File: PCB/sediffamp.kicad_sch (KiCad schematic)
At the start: 19 parts, among them U4 OPA1622

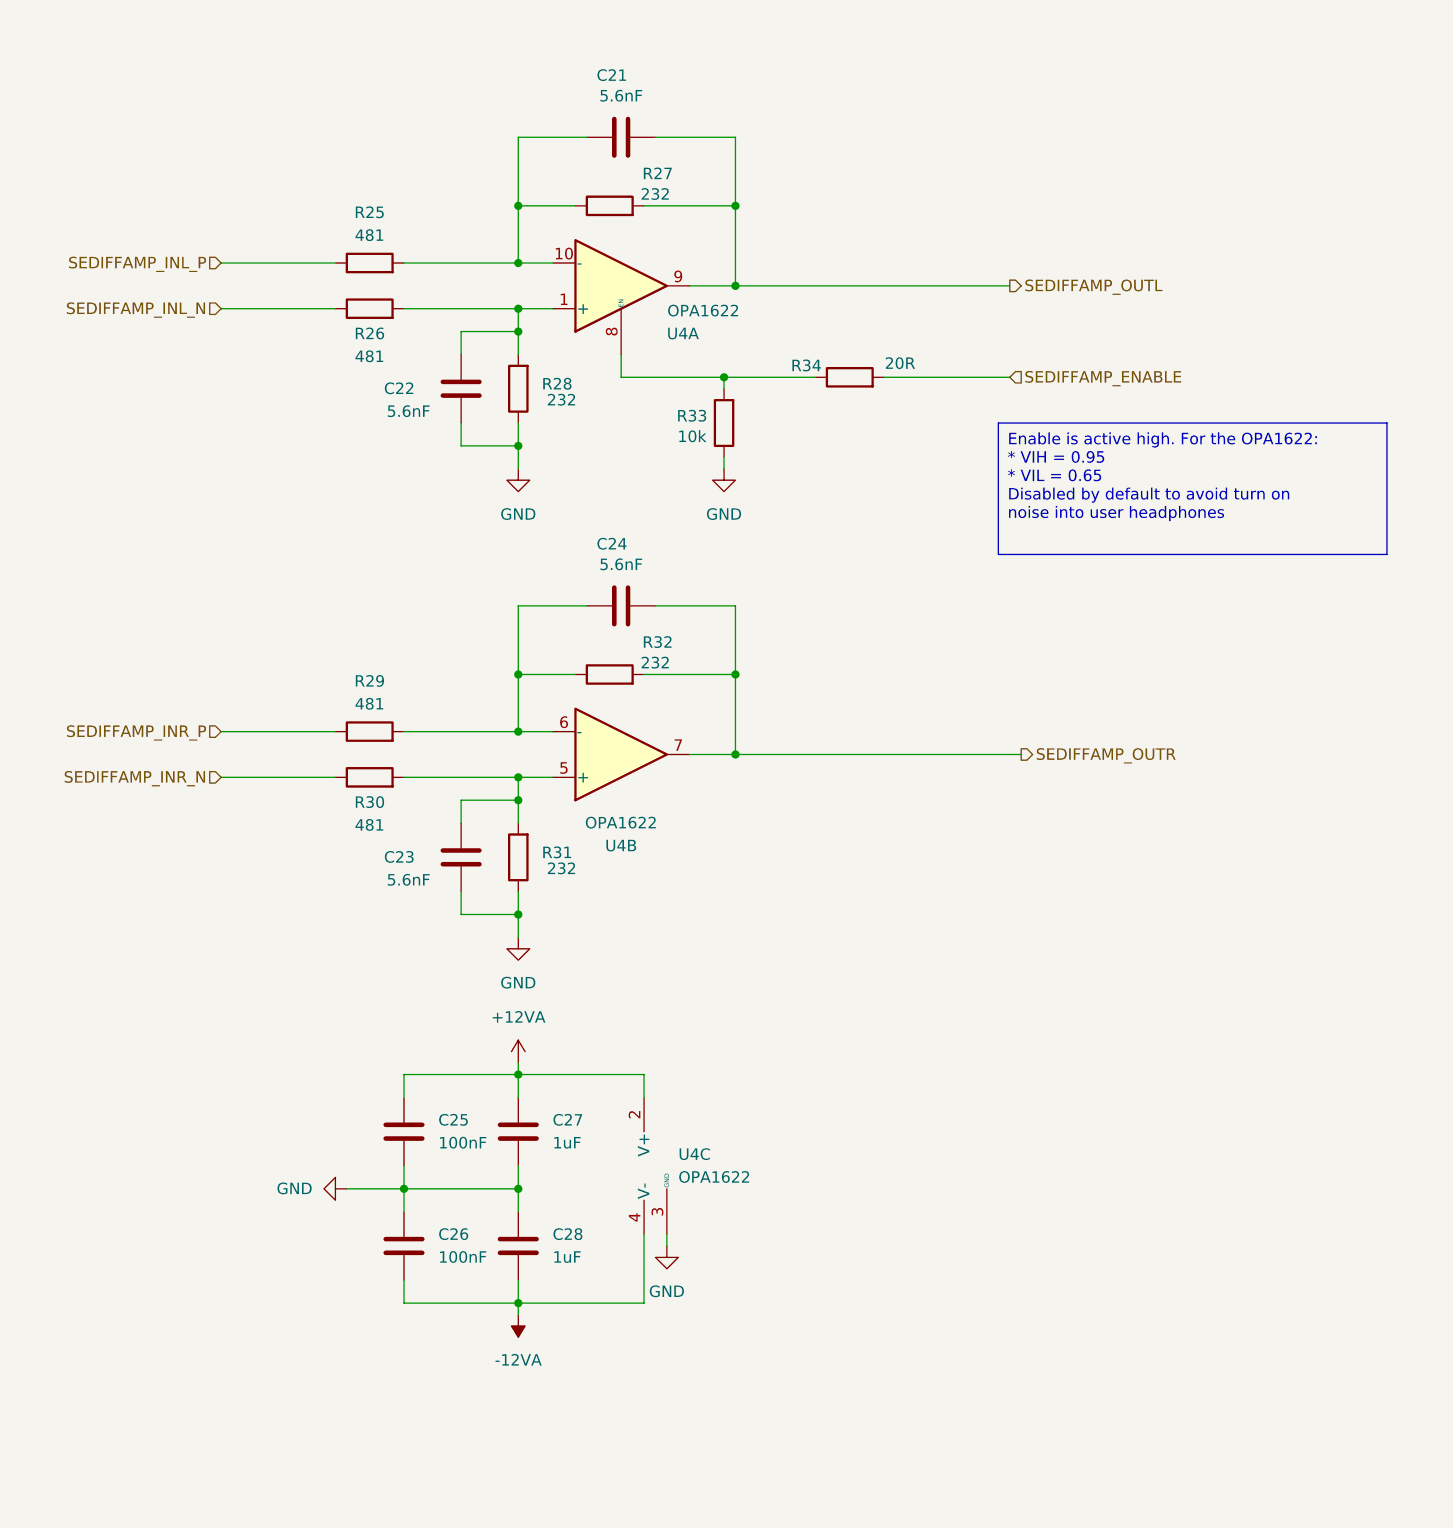
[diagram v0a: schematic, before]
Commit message: Added power supply and adjusted the AMP section to use only OPA1622 as output amp. In sync with Live 16
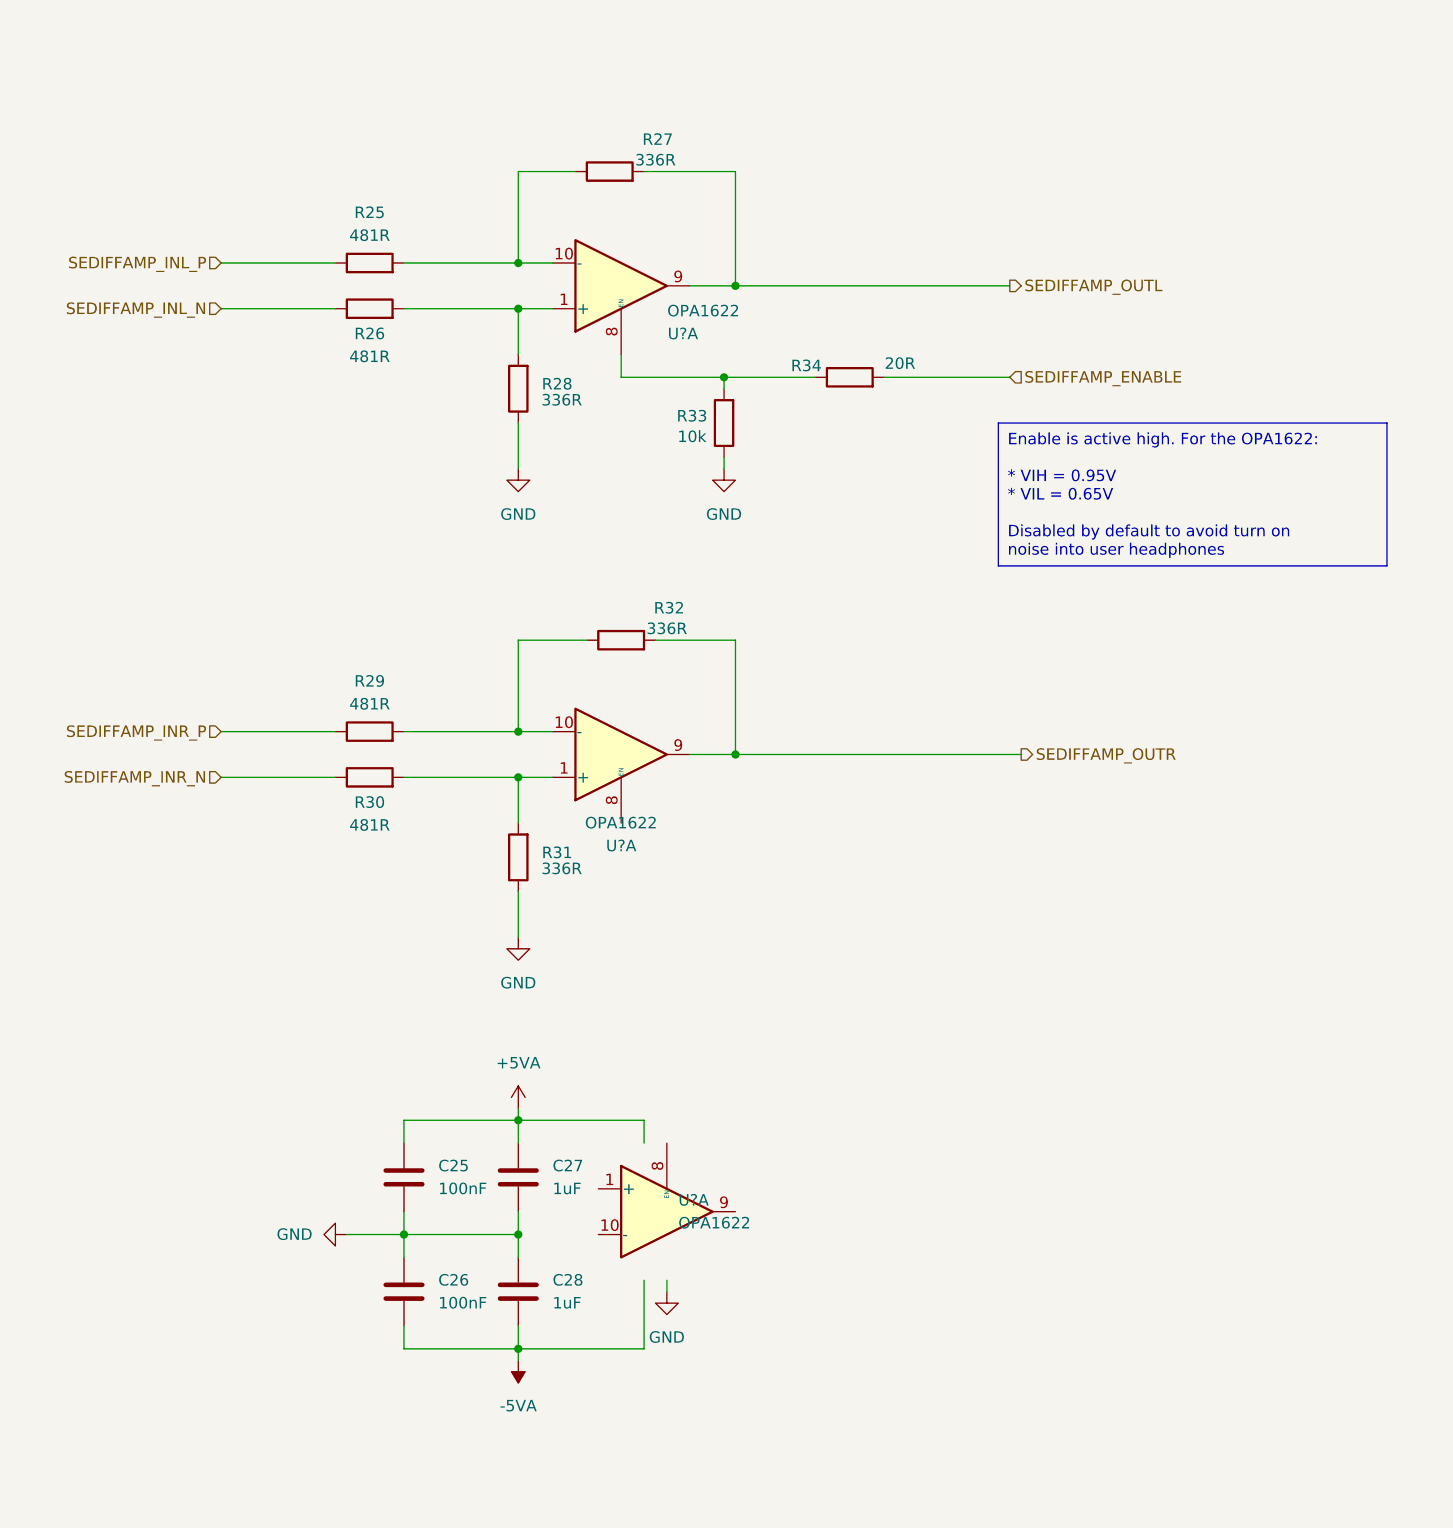
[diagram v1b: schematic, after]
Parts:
- removed C21, C22, C23, C24: 5.6nF, Capacitor_SMD:C_0402_1005Metric_Pad0.74x0.62mm_HandSolder, symbol Device:C
- C25, C26: Voltage 6.3V -> 25V
- R25, R26, R29, R30: value 481 -> 481R; Tolerance (none) -> 0.1%
- R27, R28, R31, R32: value 232 -> 336R; Tolerance (none) -> 0.1%
- renumbered U4 to U?
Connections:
- net GND: no longer U?.3 (GND)
- net SEDIFFAMP_OUTR: now also U?.9; no longer U?.7
- net at R30.2, R31.2: now also U?.1 (+); no longer U?.5 (+)
- net at R29.2, R32.1: now also U?.10 (-); no longer U?.6 (-)
- net +12VA renamed +5VA
- net +5VA: no longer U?.2 (V+)
- net -12VA renamed -5VA
- net -5VA: no longer U?.11 (V-), U?.4 (V-)
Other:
- moved on the sheet: C25, C26, C27, C28, R27, R32

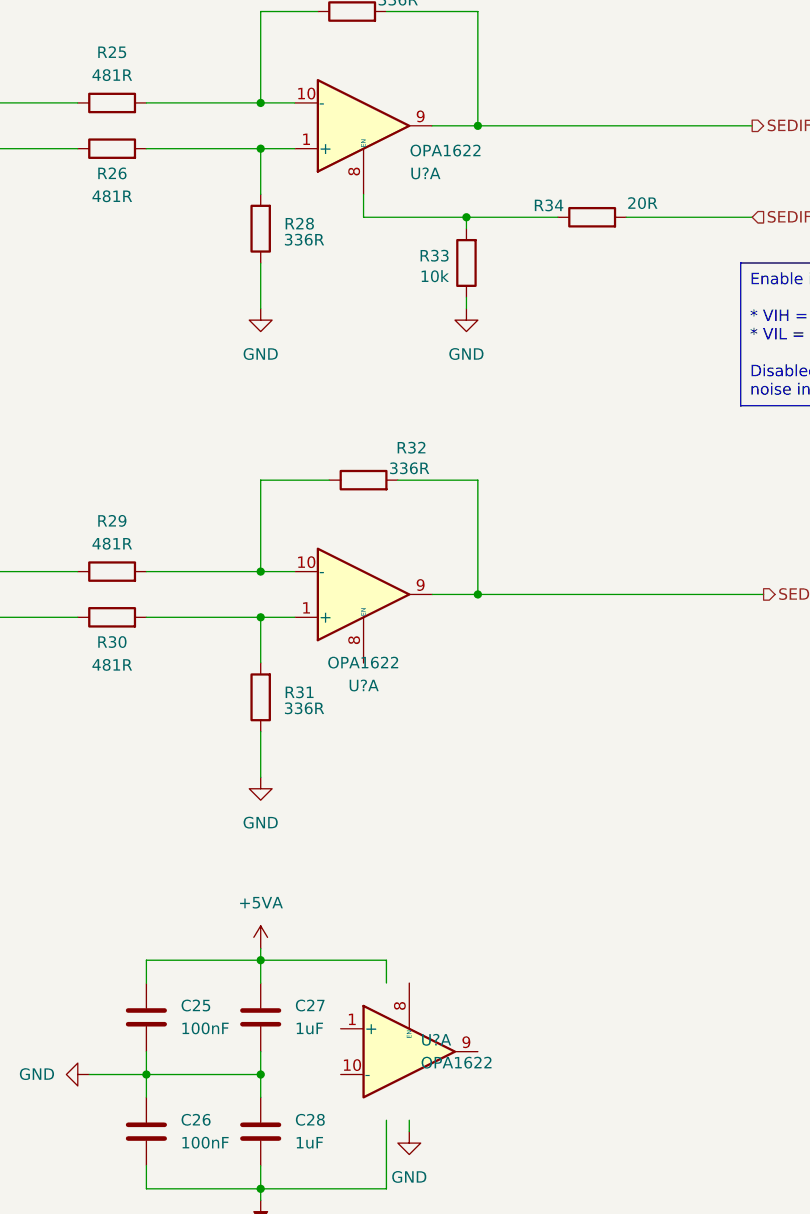
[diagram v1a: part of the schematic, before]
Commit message: Added E2P and testpoints
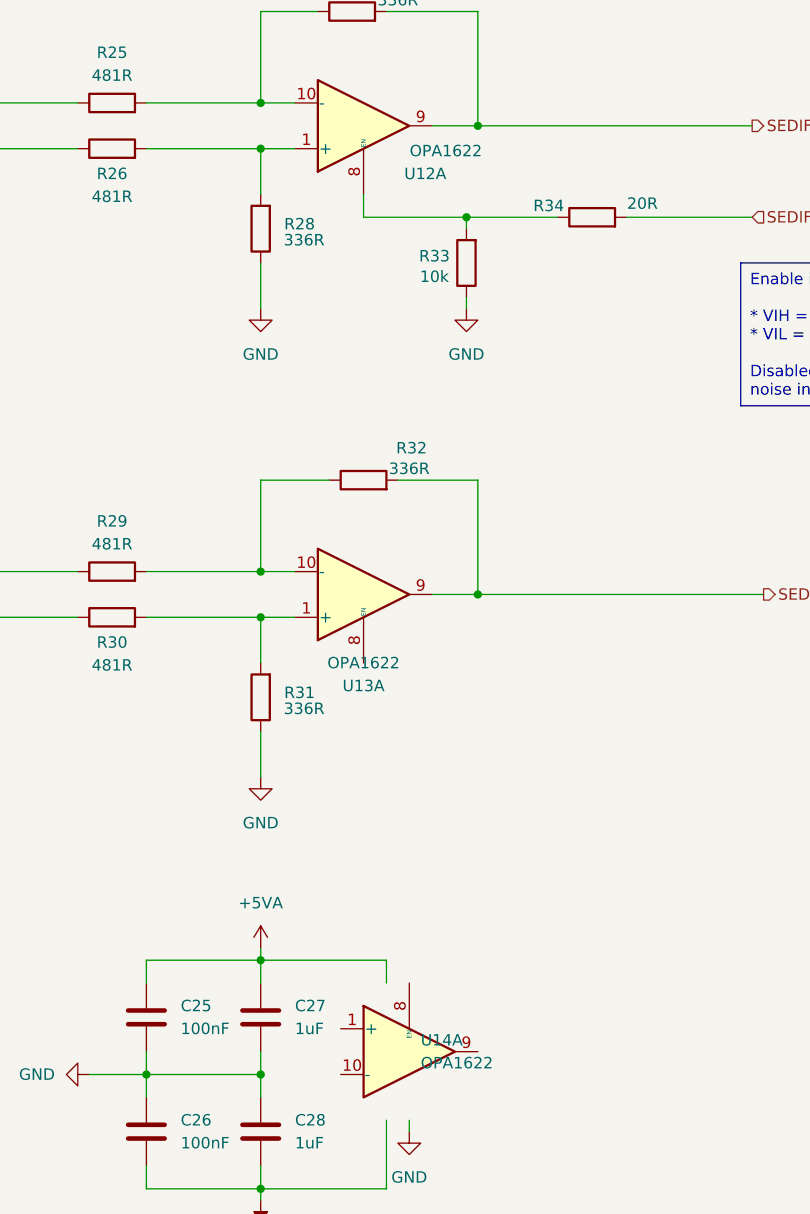
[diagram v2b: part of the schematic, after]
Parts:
- C27, C28: footprint Capacitor_SMD:C_0402_1005Metric_Pad0.74x0.62mm_HandSolder -> Capacitor_SMD:C_0603_1608Metric_Pad1.08x0.95mm_HandSolder
- gave numbers to parts that had none: 3
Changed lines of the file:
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@@
 		(dnp no)
 		(fields_autoplaced yes)
-		(property "Reference" "U?"
+		(property "Reference" "U13"
 			(at 139.7 115.57 0)
 			(effects
@@
 			(project "mhd314"
 				(path "/afee45fc-2361-4efb-9cde-757fc2efd57b/913309c3-489c-42b3-afc6-179d92cffcea/e26c83d8-adef-4edb-bc93-065fe5f245aa"
-					(reference "U?")
+					(reference "U13")
 					(unit 1)
 				)
@@
 		(on_board yes)
 		(dnp no)
-		(property "Reference" "U?"
+		(property "Reference" "U12"
 			(at 146.558 58.674 0)
 			(effects
@@
 			(project "mhd314"
 				(path "/afee45fc-2361-4efb-9cde-757fc2efd57b/913309c3-489c-42b3-afc6-179d92cffcea/e26c83d8-adef-4edb-bc93-065fe5f245aa"
-					(reference "U?")
+					(reference "U12")
 					(unit 1)
 				)
@@
 			)
 		)
-		(property "Footprint" "Capacitor_SMD:C_0402_1005Metric_Pad0.74x0.62mm_HandSolder"
+		(property "Footprint" "Capacitor_SMD:C_0603_1608Metric_Pad1.08x0.95mm_HandSolder"
 			(at 129.2352 156.21 0)
 			(effects
@@
 		(dnp no)
 		(fields_autoplaced yes)
-		(property "Reference" "#PWR?"
+		(property "Reference" "#PWR0108"
 			(at 128.27 80.01 0)
 			(effects
@@
 			(project "mhd314"
 				(path "/afee45fc-2361-4efb-9cde-757fc2efd57b/913309c3-489c-42b3-afc6-179d92cffcea/e26c83d8-adef-4edb-bc93-065fe5f245aa"
-					(reference "#PWR?")
+					(reference "#PWR0108")
 					(unit 1)
 				)
@@
 		(dnp no)
 		(fields_autoplaced yes)
-		(property "Reference" "U?"
+		(property "Reference" "U14"
 			(at 146.05 154.9399 0)
 			(effects
@@
 			(project "mhd314"
 				(path "/afee45fc-2361-4efb-9cde-757fc2efd57b/913309c3-489c-42b3-afc6-179d92cffcea/e26c83d8-adef-4edb-bc93-065fe5f245aa"
-					(reference "U?")
+					(reference "U14")
 					(unit 1)
 				)
@@
 			)
 		)
-		(property "Footprint" "Capacitor_SMD:C_0402_1005Metric_Pad0.74x0.62mm_HandSolder"
+		(property "Footprint" "Capacitor_SMD:C_0603_1608Metric_Pad1.08x0.95mm_HandSolder"
 			(at 129.2352 168.91 0)
 			(effects
